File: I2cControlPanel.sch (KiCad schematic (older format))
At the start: 55 parts, among them J1 JoystickL, J2 Conn_01x06, J3 Conn_01x04, J4 Conn_01x04, J5 JoystickR, J6 Conn_01x04, SW6 SW_Push, U1 NJM12888F33, U2 ATmega328PB-MU, U3 AQM0802

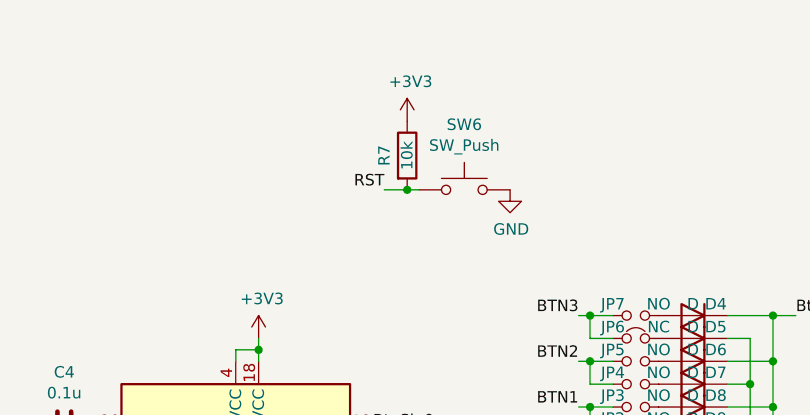
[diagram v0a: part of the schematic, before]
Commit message: Remove R7 resistor
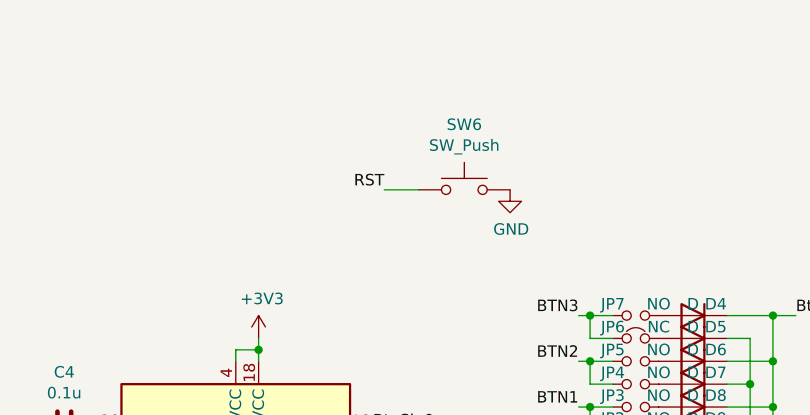
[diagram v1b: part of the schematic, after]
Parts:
- removed R7: 10k, Resistor_SMD:R_0603_1608Metric, symbol Device:R
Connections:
- wire segments 118 -> 117
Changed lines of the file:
@@
 Wire Wire Line
 	7950 5050 8550 5050
-$Comp
-L Device:R R7
-U 1 1 5F378607
-P 6600 1400
-F 0 "R7" V 6500 1400 50  0000 C CNN
-F 1 "10k" V 6600 1400 50  0000 C CNN
-F 2 "Resistor_SMD:R_0603_1608Metric" V 6530 1400 50  0001 C CNN
-F 3 "~" H 6600 1400 50  0001 C CNN
-	1    6600 1400
-	1    0    0    -1
-$EndComp
-Wire Wire Line
-	6500 1550 6600 1550
-Connection ~ 6600 1550
-Wire Wire Line
-	6600 1550 6650 1550
-$Comp
-L power:+3V3 #PWR0132
-U 1 1 5F381188
-P 6600 1250
-F 0 "#PWR0132" H 6600 1100 50  0001 C CNN
-F 1 "+3V3" H 6615 1423 50  0000 C CNN
-F 2 "" H 6600 1250 50  0001 C CNN
-F 3 "" H 6600 1250 50  0001 C CNN
-	1    6600 1250
-	1    0    0    -1
-$EndComp
 Wire Wire Line
 	2550 1000 2550 1100
@@
 Wire Wire Line
 	4150 4050 4150 4250
+Wire Wire Line
+	6500 1550 6650 1550
 $EndSCHEMATC

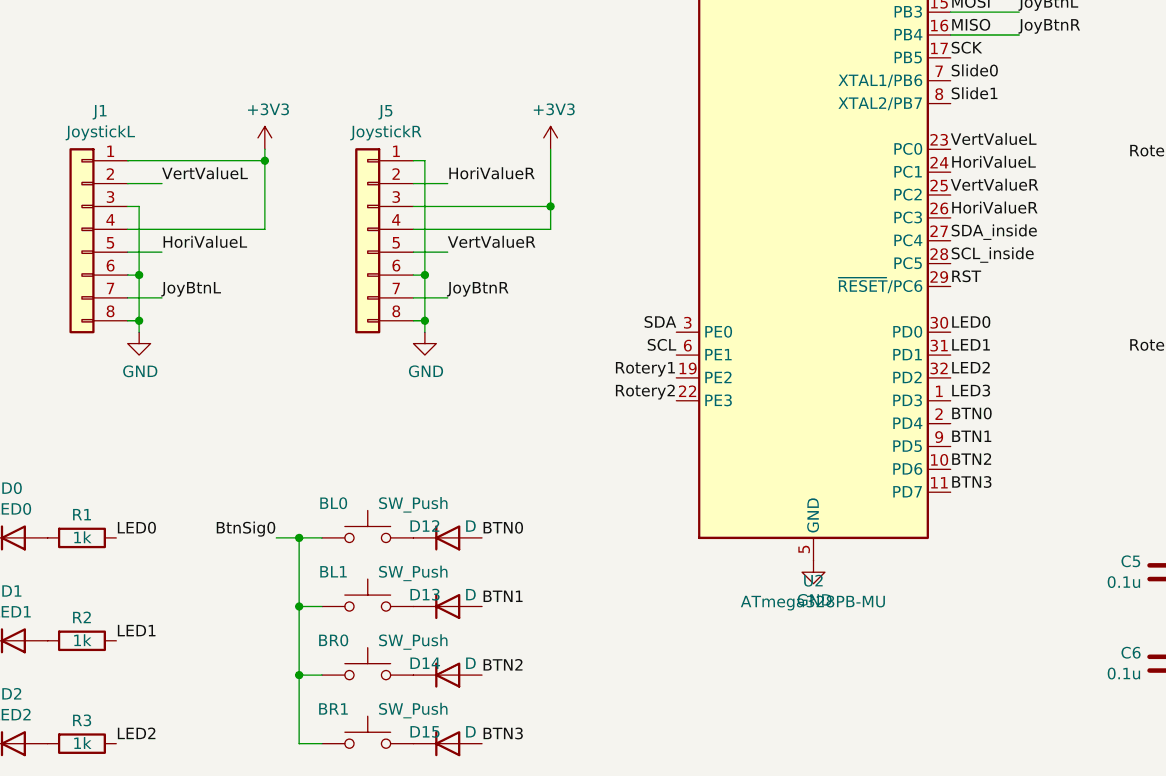
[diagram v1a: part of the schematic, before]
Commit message: Replace vert and hori for joy
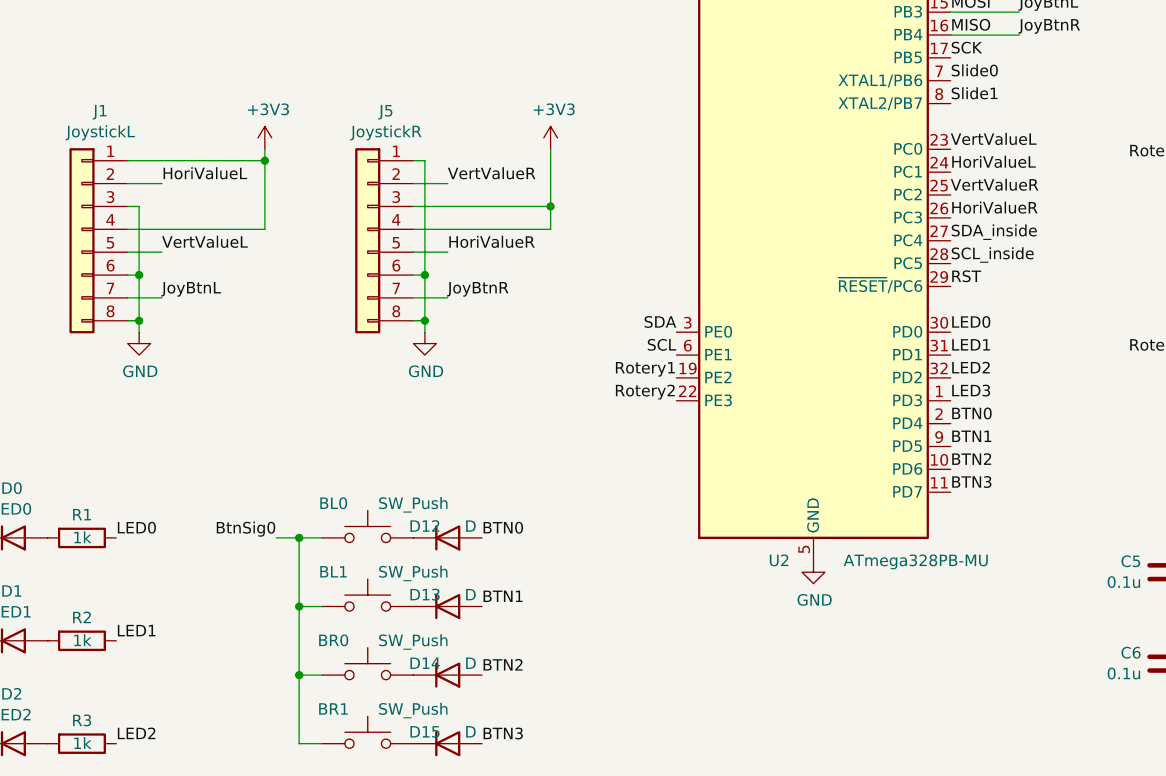
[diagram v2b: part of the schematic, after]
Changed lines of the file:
@@
 	1    0    0    -1
 $EndComp
+Text Label 3000 3950 0    50   ~ 0
+VertValueL
 Text Label 3000 3650 0    50   ~ 0
-VertValueL
-Text Label 3000 3950 0    50   ~ 0
 HoriValueL
 Wire Wire Line
@@
 U 1 1 5ECFEE32
 P 5850 3800
-F 0 "U2" H 5850 2211 50  0000 C CNN
-F 1 "ATmega328PB-MU" H 5850 2120 50  0000 C CNN
+F 0 "U2" H 5700 2300 50  0000 C CNN
+F 1 "ATmega328PB-MU" H 6300 2300 50  0000 C CNN
 F 2 "Package_DFN_QFN:QFN-32-1EP_5x5mm_P0.5mm_EP3.1x3.1mm" H 5850 3800 50  0001 C CIN
 F 3 "http://ww1.microchip.com/downloads/en/DeviceDoc/40001906C.pdf" H 5850 3800 50  0001 C CNN
@@
 	1    0    0    -1
 $EndComp
+Text Label 4250 3650 0    50   ~ 0
+VertValueR
 Text Label 4250 3950 0    50   ~ 0
-VertValueR
-Text Label 4250 3650 0    50   ~ 0
 HoriValueR
 Wire Wire Line

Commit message: Change pad for diode
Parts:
- D10, D11, D12, D13, D14, D15, D4, D5, D6, D7, D8, D9: footprint Diode_SMD:D_SOD-323 -> my-kicad-footprints:D_SOD-523F
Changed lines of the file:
@@
 F 0 "D6" H 7750 2250 50  0000 C CNN
 F 1 "D" H 7850 2250 50  0000 C CNN
-F 2 "Diode_SMD:D_SOD-323" H 7850 2300 50  0001 C CNN
+F 2 "my-kicad-footprints:D_SOD-523F" H 7850 2300 50  0001 C CNN
 F 3 "~" H 7850 2300 50  0001 C CNN
 	1    7850 2300
@@
 F 0 "D7" H 7750 2350 50  0000 C CNN
 F 1 "D" H 7850 2350 50  0000 C CNN
-F 2 "Diode_SMD:D_SOD-323" H 7850 2400 50  0001 C CNN
+F 2 "my-kicad-footprints:D_SOD-523F" H 7850 2400 50  0001 C CNN
 F 3 "~" H 7850 2400 50  0001 C CNN
 	1    7850 2400
@@
 F 0 "D8" H 7750 2450 50  0000 C CNN
 F 1 "D" H 7850 2450 50  0000 C CNN
-F 2 "Diode_SMD:D_SOD-323" H 7850 2500 50  0001 C CNN
+F 2 "my-kicad-footprints:D_SOD-523F" H 7850 2500 50  0001 C CNN
 F 3 "~" H 7850 2500 50  0001 C CNN
 	1    7850 2500
@@
 F 0 "D9" H 7750 2550 50  0000 C CNN
 F 1 "D" H 7850 2550 50  0000 C CNN
-F 2 "Diode_SMD:D_SOD-323" H 7850 2600 50  0001 C CNN
+F 2 "my-kicad-footprints:D_SOD-523F" H 7850 2600 50  0001 C CNN
 F 3 "~" H 7850 2600 50  0001 C CNN
 	1    7850 2600
@@
 F 0 "D10" H 7750 2650 50  0000 C CNN
 F 1 "D" H 7850 2650 50  0000 C CNN
-F 2 "Diode_SMD:D_SOD-323" H 7850 2700 50  0001 C CNN
+F 2 "my-kicad-footprints:D_SOD-523F" H 7850 2700 50  0001 C CNN
 F 3 "~" H 7850 2700 50  0001 C CNN
 	1    7850 2700
@@
 F 0 "D11" H 7750 2750 50  0000 C CNN
 F 1 "D" H 7850 2750 50  0000 C CNN
-F 2 "Diode_SMD:D_SOD-323" H 7850 2800 50  0001 C CNN
+F 2 "my-kicad-footprints:D_SOD-523F" H 7850 2800 50  0001 C CNN
 F 3 "~" H 7850 2800 50  0001 C CNN
 	1    7850 2800
@@
 F 0 "D5" H 7750 2150 50  0000 C CNN
 F 1 "D" H 7850 2150 50  0000 C CNN
-F 2 "Diode_SMD:D_SOD-323" H 7850 2200 50  0001 C CNN
+F 2 "my-kicad-footprints:D_SOD-523F" H 7850 2200 50  0001 C CNN
 F 3 "~" H 7850 2200 50  0001 C CNN
 	1    7850 2200
@@
 F 0 "D4" H 7750 2050 50  0000 C CNN
 F 1 "D" H 7850 2050 50  0000 C CNN
-F 2 "Diode_SMD:D_SOD-323" H 7850 2100 50  0001 C CNN
+F 2 "my-kicad-footprints:D_SOD-523F" H 7850 2100 50  0001 C CNN
 F 3 "~" H 7850 2100 50  0001 C CNN
 	1    7850 2100
@@
 F 0 "D12" H 4150 5150 50  0000 C CNN
 F 1 "D" H 4350 5150 50  0000 C CNN
-F 2 "Diode_SMD:D_SOD-323" H 4250 5200 50  0001 C CNN
+F 2 "my-kicad-footprints:D_SOD-523F" H 4250 5200 50  0001 C CNN
 F 3 "~" H 4250 5200 50  0001 C CNN
 	1    4250 5200
@@
 F 0 "D13" H 4150 5450 50  0000 C CNN
 F 1 "D" H 4350 5450 50  0000 C CNN
-F 2 "Diode_SMD:D_SOD-323" H 4250 5500 50  0001 C CNN
+F 2 "my-kicad-footprints:D_SOD-523F" H 4250 5500 50  0001 C CNN
 F 3 "~" H 4250 5500 50  0001 C CNN
 	1    4250 5500
@@
 F 0 "D14" H 4150 5750 50  0000 C CNN
 F 1 "D" H 4350 5750 50  0000 C CNN
-F 2 "Diode_SMD:D_SOD-323" H 4250 5800 50  0001 C CNN
+F 2 "my-kicad-footprints:D_SOD-523F" H 4250 5800 50  0001 C CNN
 F 3 "~" H 4250 5800 50  0001 C CNN
 	1    4250 5800
@@
 F 0 "D15" H 4150 6050 50  0000 C CNN
 F 1 "D" H 4350 6050 50  0000 C CNN
-F 2 "Diode_SMD:D_SOD-323" H 4250 6100 50  0001 C CNN
+F 2 "my-kicad-footprints:D_SOD-523F" H 4250 6100 50  0001 C CNN
 F 3 "~" H 4250 6100 50  0001 C CNN
 	1    4250 6100

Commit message: Update pad of led for soldering by hand
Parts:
- D0, D1, D2, D3: footprint Diode_SMD:D_0603_1608Metric -> Diode_SMD:D_0603_1608Metric_Pad1.05x0.95mm_HandSolder
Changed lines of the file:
@@
 F 0 "D0" H 2343 5416 50  0000 C CNN
 F 1 "LED0" H 2343 5325 50  0000 C CNN
-F 2 "Diode_SMD:D_0603_1608Metric" H 2350 5200 50  0001 C CNN
+F 2 "Diode_SMD:D_0603_1608Metric_Pad1.05x0.95mm_HandSolder" H 2350 5200 50  0001 C CNN
 F 3 "~" H 2350 5200 50  0001 C CNN
 	1    2350 5200
@@
 F 0 "D1" H 2343 5866 50  0000 C CNN
 F 1 "LED1" H 2343 5775 50  0000 C CNN
-F 2 "Diode_SMD:D_0603_1608Metric" H 2350 5650 50  0001 C CNN
+F 2 "Diode_SMD:D_0603_1608Metric_Pad1.05x0.95mm_HandSolder" H 2350 5650 50  0001 C CNN
 F 3 "~" H 2350 5650 50  0001 C CNN
 	1    2350 5650
@@
 F 0 "D2" H 2343 6316 50  0000 C CNN
 F 1 "LED2" H 2343 6225 50  0000 C CNN
-F 2 "Diode_SMD:D_0603_1608Metric" H 2350 6100 50  0001 C CNN
+F 2 "Diode_SMD:D_0603_1608Metric_Pad1.05x0.95mm_HandSolder" H 2350 6100 50  0001 C CNN
 F 3 "~" H 2350 6100 50  0001 C CNN
 	1    2350 6100
@@
 F 0 "D3" H 2343 6766 50  0000 C CNN
 F 1 "LED3" H 2343 6675 50  0000 C CNN
-F 2 "Diode_SMD:D_0603_1608Metric" H 2350 6550 50  0001 C CNN
+F 2 "Diode_SMD:D_0603_1608Metric_Pad1.05x0.95mm_HandSolder" H 2350 6550 50  0001 C CNN
 F 3 "~" H 2350 6550 50  0001 C CNN
 	1    2350 6550

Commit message: Change slide switch
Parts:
- Slide0, Slide1: footprint my-kicad-footprints:SlideSwitch -> my-kicad-footprints:SlideSwitch_SS12D01G4_2posi_1line; symbol Switch:SW_Push_DPDT -> Switch:SW_SPDT
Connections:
- no-connect marks 9 -> 3
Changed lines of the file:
@@
 Text Label 6450 3300 0    50   ~ 0
 Slide1
-NoConn ~ 10550 1800
 Text Label 6450 4600 0    50   ~ 0
 LED3
@@
 Wire Wire Line
 	8100 2200 8000 2200
-NoConn ~ 10150 1700
-NoConn ~ 10550 1600
-Text Label 10150 1300 2    50   ~ 0
+Text Label 10150 1750 2    50   ~ 0
 Slide0
 $Comp
 L power:GND #PWR0117
 U 1 1 5EEC7434
-P 10650 1200
-F 0 "#PWR0117" H 10650 950 50  0001 C CNN
-F 1 "GND" H 10655 1027 50  0000 C CNN
-F 2 "" H 10650 1200 50  0001 C CNN
-F 3 "" H 10650 1200 50  0001 C CNN
-	1    10650 1200
-	1    0    0    -1
-$EndComp
-$Comp
-L Switch:SW_Push_DPDT Slide0
+P 10650 1650
+F 0 "#PWR0117" H 10650 1400 50  0001 C CNN
+F 1 "GND" H 10655 1477 50  0000 C CNN
+F 2 "" H 10650 1650 50  0001 C CNN
+F 3 "" H 10650 1650 50  0001 C CNN
+	1    10650 1650
+	1    0    0    -1
+$EndComp
+$Comp
+L Switch:SW_SPDT Slide0
 U 1 1 5EEC5D06
-P 10350 1500
-F 0 "Slide0" H 10350 1985 50  0000 C CNN
-F 1 "SlideSwitch" H 10350 1894 50  0000 C CNN
-F 2 "my-kicad-footprints:SlideSwitch" H 10350 1700 50  0001 C CNN
-F 3 "~" H 10350 1700 50  0001 C CNN
-	1    10350 1500
-	1    0    0    -1
-$EndComp
-NoConn ~ 10550 2850
-NoConn ~ 10150 2750
-NoConn ~ 10550 2650
+P 10350 1750
+F 0 "Slide0" H 10350 2050 50  0000 C CNN
+F 1 "SlideSwitch" H 10350 1950 50  0000 C CNN
+F 2 "my-kicad-footprints:SlideSwitch_SS12D01G4_2posi_1line" H 10350 1950 50  0001 C CNN
+F 3 "~" H 10350 1950 50  0001 C CNN
+	1    10350 1750
+	1    0    0    -1
+$EndComp
 Text Label 10150 2350 2    50   ~ 0
 Slide1
@@
 $EndComp
 $Comp
-L Switch:SW_Push_DPDT Slide1
+L Switch:SW_SPDT Slide1
 U 1 1 5F41D1BB
-P 10350 2550
-F 0 "Slide1" H 10350 3035 50  0000 C CNN
-F 1 "SlideSwitch" H 10350 2944 50  0000 C CNN
-F 2 "my-kicad-footprints:SlideSwitch" H 10350 2750 50  0001 C CNN
-F 3 "~" H 10350 2750 50  0001 C CNN
-	1    10350 2550
-	1    0    0    -1
-$EndComp
-NoConn ~ 10550 1400
+P 10350 2350
+F 0 "Slide1" H 10350 2650 50  0000 C CNN
+F 1 "SlideSwitch" H 10350 2550 50  0000 C CNN
+F 2 "my-kicad-footprints:SlideSwitch_SS12D01G4_2posi_1line" H 10350 2550 50  0001 C CNN
+F 3 "~" H 10350 2550 50  0001 C CNN
+	1    10350 2350
+	1    0    0    -1
+$EndComp
+NoConn ~ 10550 1850
 NoConn ~ 10550 2450
 $Comp
@@
 $EndComp
 Wire Wire Line
-	10650 1200 10550 1200
+	10650 1650 10550 1650
 Wire Wire Line
 	10550 2250 10650 2250

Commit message: Plot schematic as pdf
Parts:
- Encoder0, Encoder1: symbol Device:R_POT_US -> I2cControlPanel-rescue:R_POT_US-Device
- JP0, JP1, JP2, JP3, JP4, JP5, JP7: symbol Device:Jumper_NO_Small -> I2cControlPanel-rescue:Jumper_NO_Small-Device
- JP6: symbol Device:Jumper_NC_Small -> I2cControlPanel-rescue:Jumper_NC_Small-Device
- U2: symbol MCU_Microchip_ATmega:ATmega328PB-MU -> I2cControlPanel-rescue:ATmega328PB-MU-MCU_Microchip_ATmega
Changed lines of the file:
@@
 	9150 2350 9450 2350
 $Comp
-L MCU_Microchip_ATmega:ATmega328PB-MU U2
+L I2cControlPanel-rescue:ATmega328PB-MU-MCU_Microchip_ATmega U2
 U 1 1 5ECFEE32
 P 5850 3800
@@
 $EndComp
 $Comp
-L Device:R_POT_US Encoder0
+L I2cControlPanel-rescue:R_POT_US-Device Encoder0
 U 1 1 5EE7F6DB
 P 7700 3550
@@
 	7500 3550 7550 3550
 $Comp
-L Device:R_POT_US Encoder1
+L I2cControlPanel-rescue:R_POT_US-Device Encoder1
 U 1 1 5EE88740
 P 7700 4400
@@
 	3000 4150 2850 4150
 $Comp
-L Device:Jumper_NC_Small JP6
+L I2cControlPanel-rescue:Jumper_NC_Small-Device JP6
 U 1 1 5EEC83B2
 P 7600 2200
@@
 $EndComp
 $Comp
-L Device:Jumper_NO_Small JP2
+L I2cControlPanel-rescue:Jumper_NO_Small-Device JP2
 U 1 1 5EEC8D64
 P 7600 2600
@@
 $EndComp
 $Comp
-L Device:Jumper_NO_Small JP5
+L I2cControlPanel-rescue:Jumper_NO_Small-Device JP5
 U 1 1 5EECEA4D
 P 7600 2300
@@
 $EndComp
 $Comp
-L Device:Jumper_NO_Small JP4
+L I2cControlPanel-rescue:Jumper_NO_Small-Device JP4
 U 1 1 5EECEC1A
 P 7600 2400
@@
 $EndComp
 $Comp
-L Device:Jumper_NO_Small JP3
+L I2cControlPanel-rescue:Jumper_NO_Small-Device JP3
 U 1 1 5EECEDB0
 P 7600 2500
@@
 $EndComp
 $Comp
-L Device:Jumper_NO_Small JP1
+L I2cControlPanel-rescue:Jumper_NO_Small-Device JP1
 U 1 1 5EECFE4F
 P 7600 2700
@@
 $EndComp
 $Comp
-L Device:Jumper_NO_Small JP0
+L I2cControlPanel-rescue:Jumper_NO_Small-Device JP0
 U 1 1 5EED0549
 P 7600 2800
@@
 $EndComp
 $Comp
-L Device:Jumper_NO_Small JP7
+L I2cControlPanel-rescue:Jumper_NO_Small-Device JP7
 U 1 1 5EED2155
 P 7600 2100
